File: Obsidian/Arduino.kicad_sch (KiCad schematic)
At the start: 25 parts

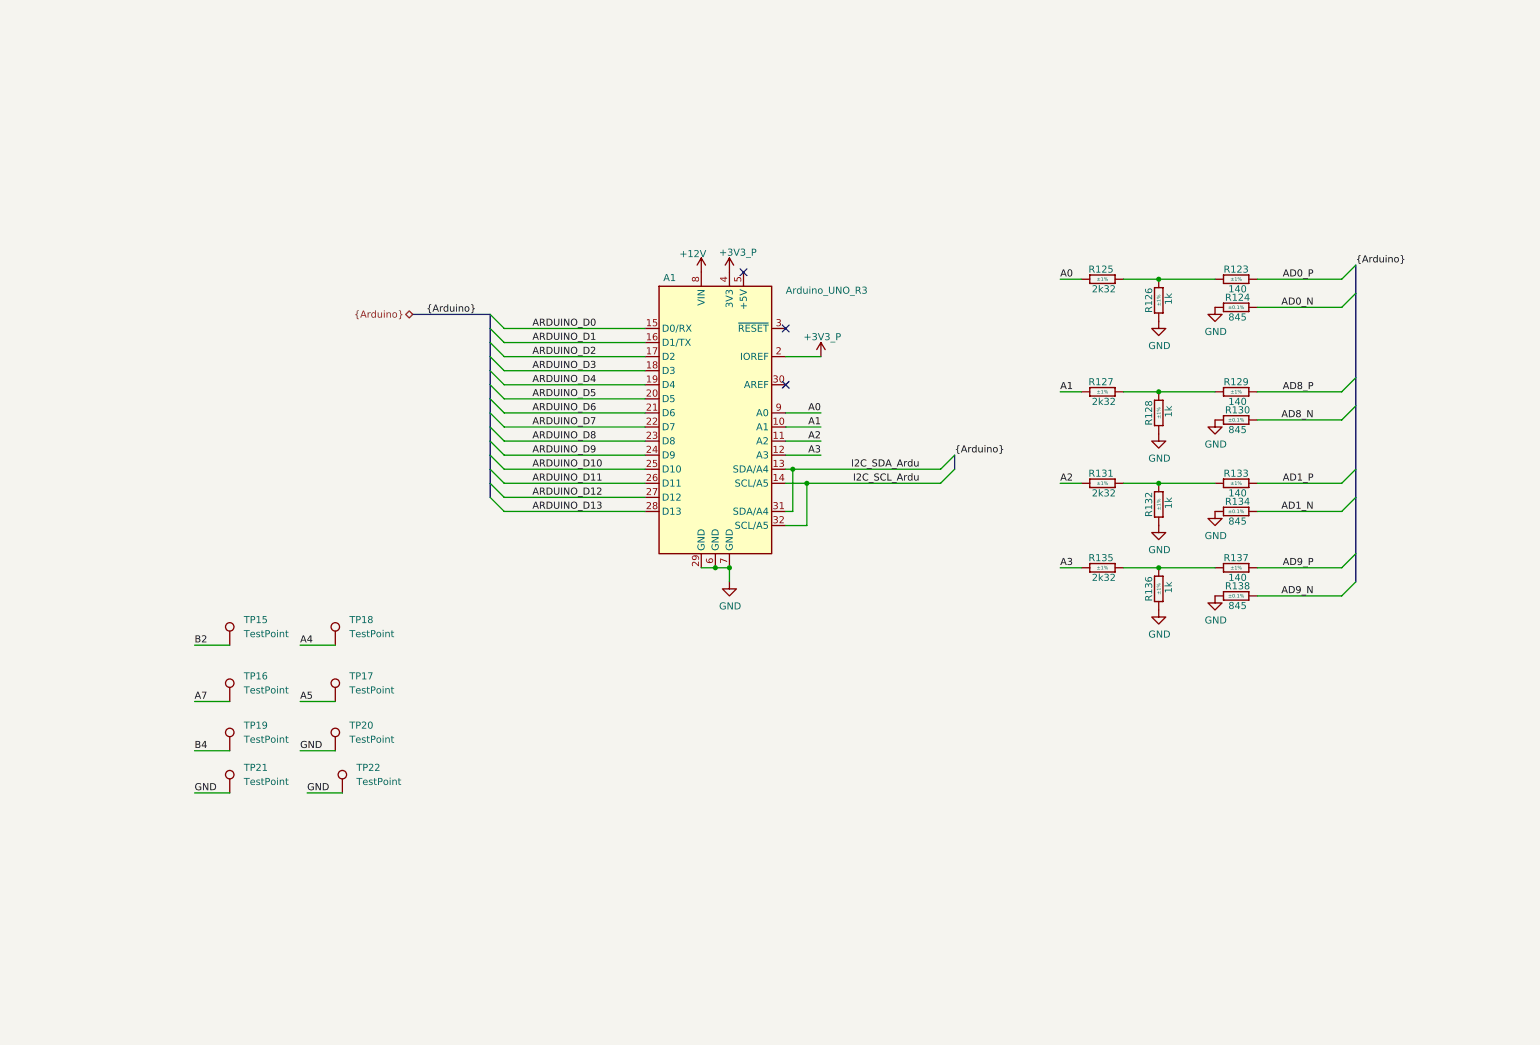
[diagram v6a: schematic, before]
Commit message: adding flex connector
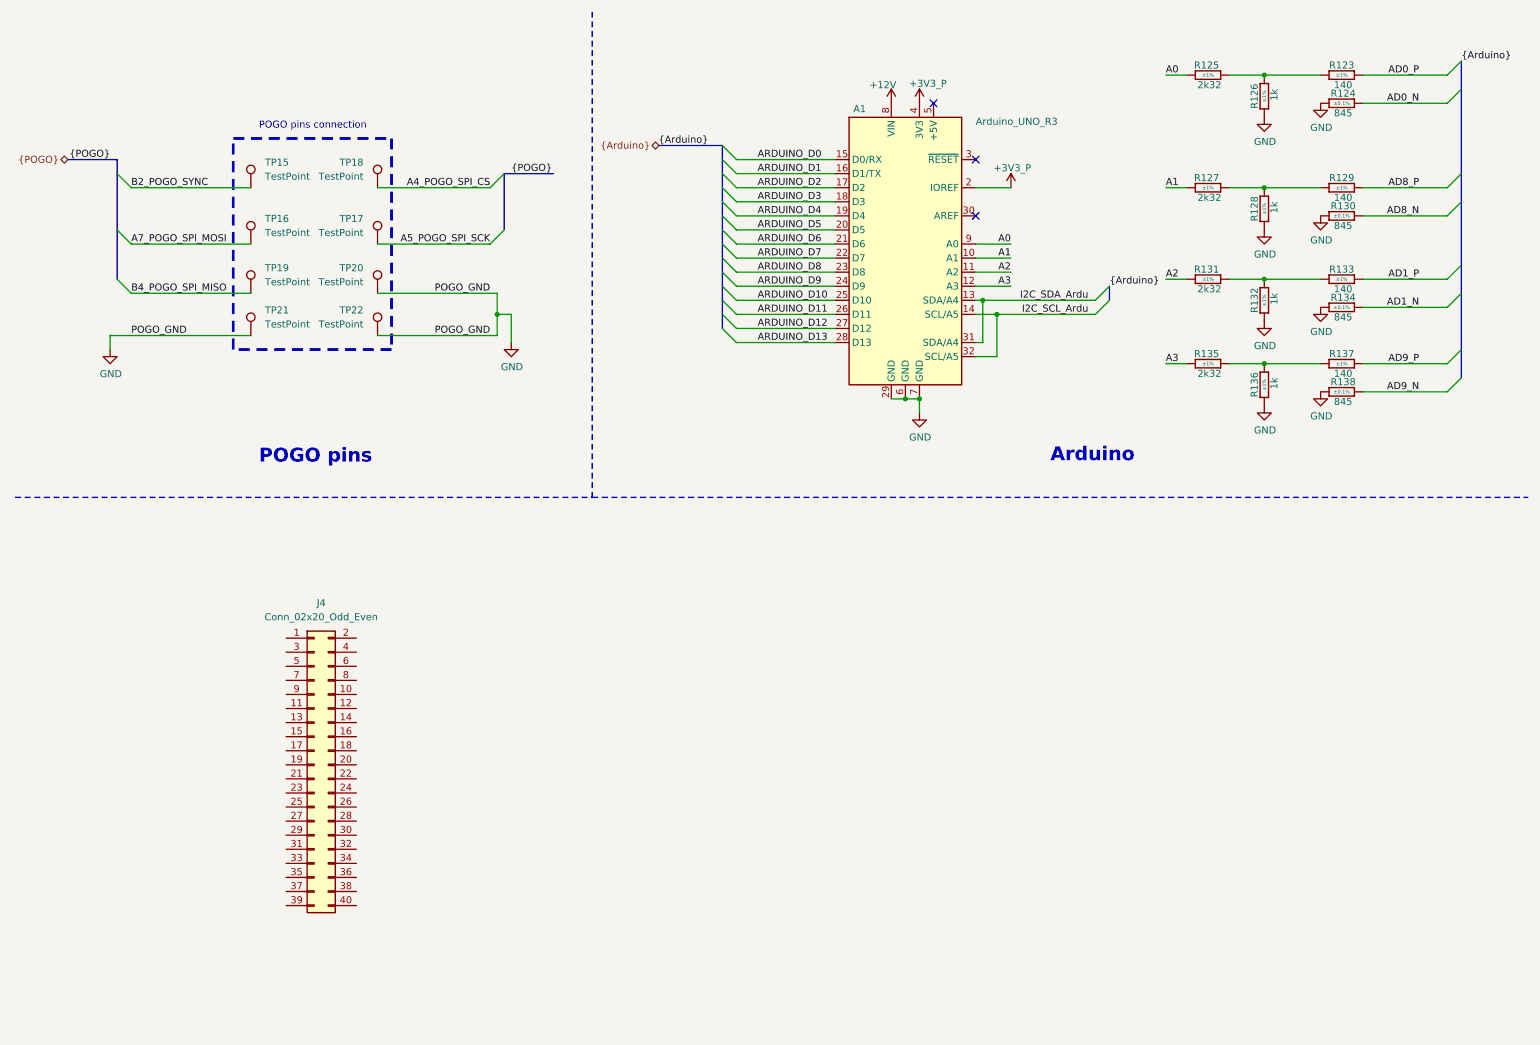
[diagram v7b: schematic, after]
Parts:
- added J4: Conn_02x20_Odd_Even, Footprint:CONN-SMD_YXT-BB10-40S-02, symbol Connector_Generic:Conn_02x20_Odd_Even
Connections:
- net A4 renamed A4_POGO_SPI_CS
- net A5 renamed A5_POGO_SPI_SCK
- net A7 renamed A7_POGO_SPI_MOSI
- net B2 renamed B2_POGO_SYNC
- net B4 renamed B4_POGO_SPI_MISO
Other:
- note added: "Arduino"
- note added: "POGO pins"
- note added: "POGO pins connection"
- moved on the sheet: A1, R123, R124, R125, R126, R127, R128, R129, R130, R131, R132, R133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

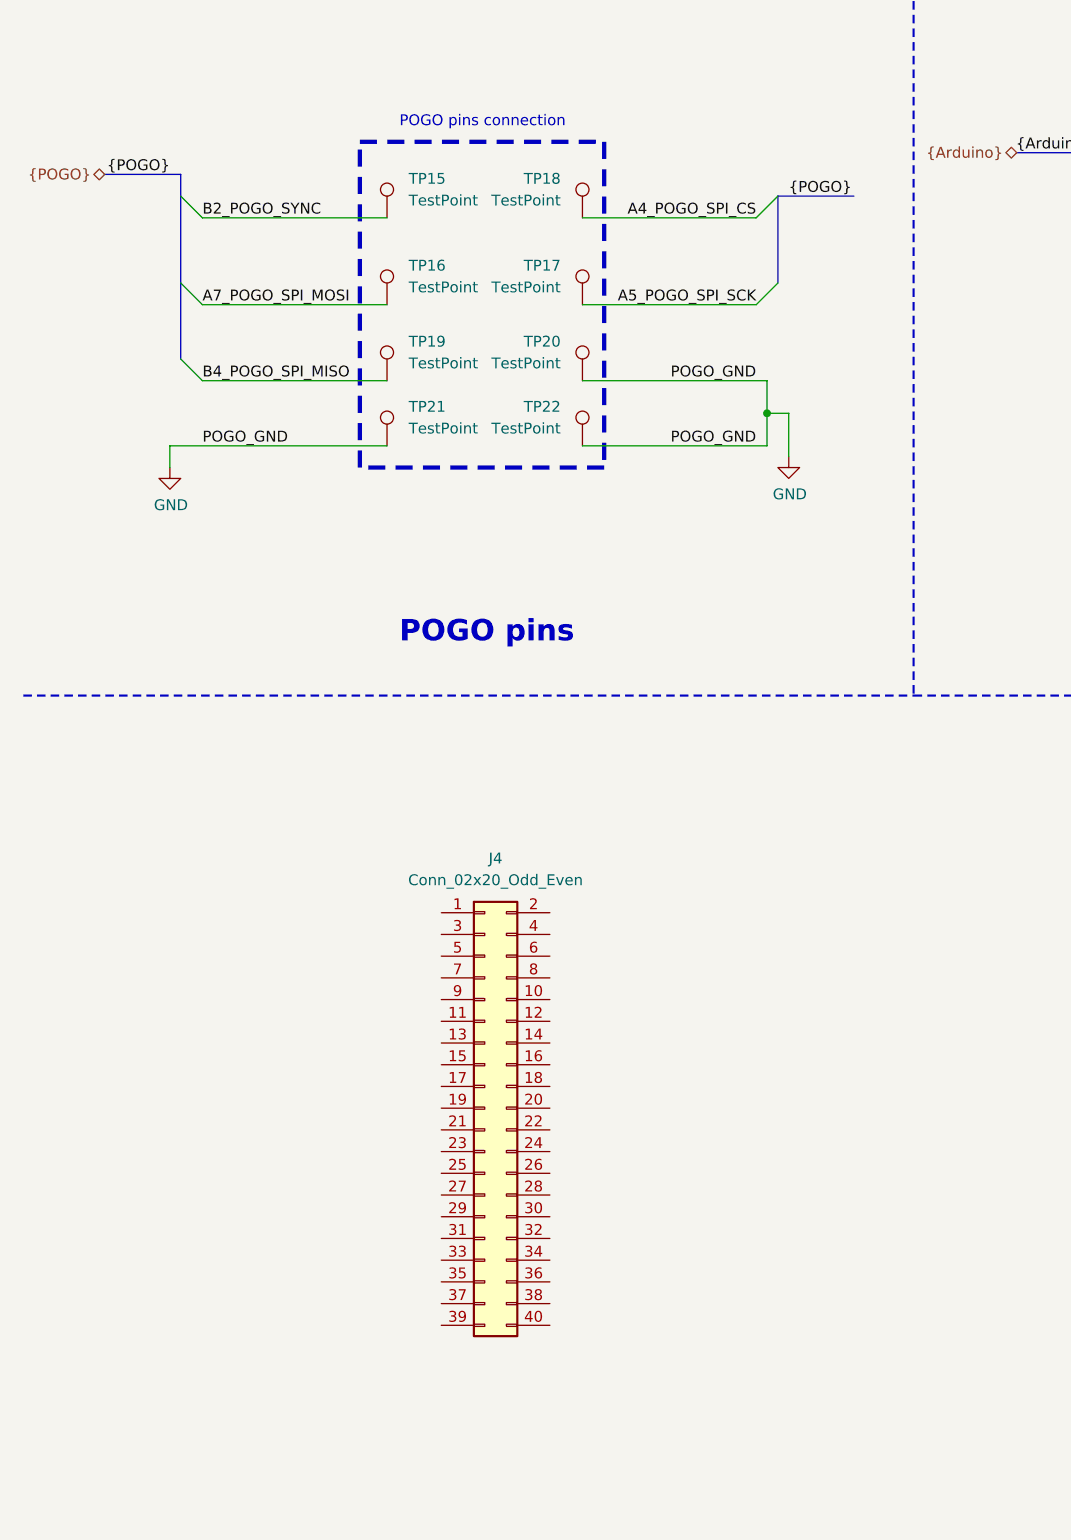
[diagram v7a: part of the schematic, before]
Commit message: Cleanup of the schematic
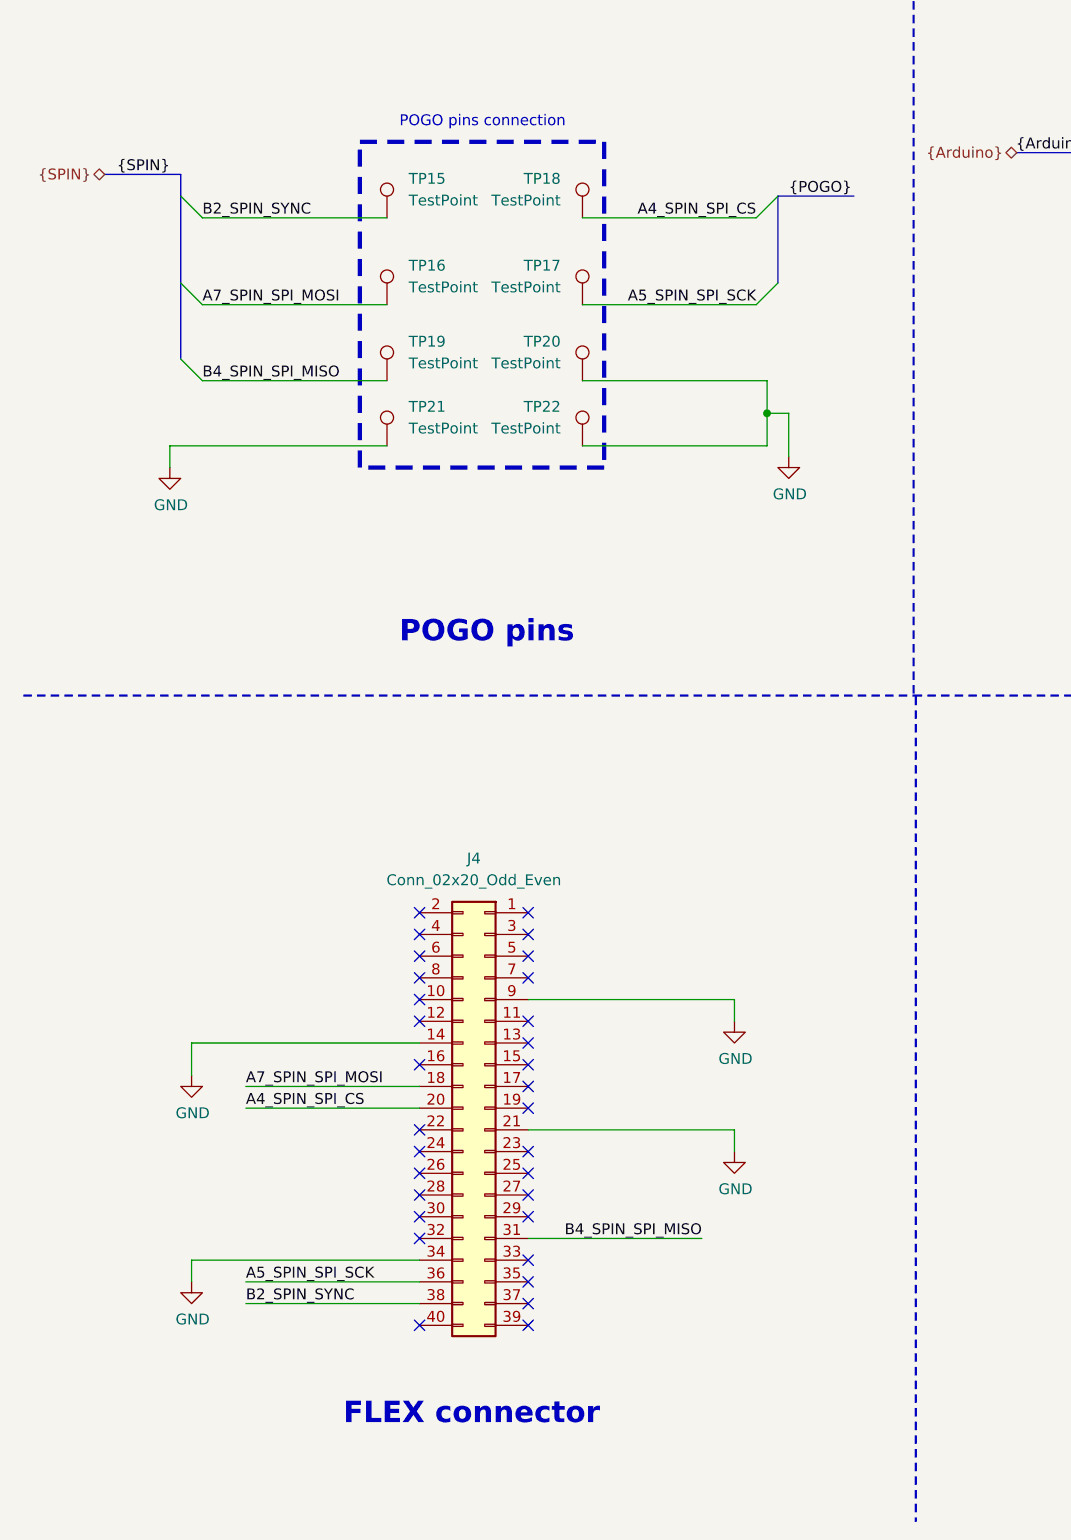
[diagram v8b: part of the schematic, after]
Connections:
- net A4_POGO_SPI_CS is gone; now on net A4_SPIN_SPI_CS: TP18.1
- net A5_POGO_SPI_SCK is gone; now on net A5_SPIN_SPI_SCK: TP17.1
- net A7_POGO_SPI_MOSI is gone; now on net A7_SPIN_SPI_MOSI: TP16.1
- net B2_POGO_SYNC is gone; now on net B2_SPIN_SYNC: TP15.1
- net B4_POGO_SPI_MISO is gone; now on net B4_SPIN_SPI_MISO: TP19.1
- net GND: now also J4.14 (Pin_14), J4.21 (Pin_21), J4.34 (Pin_34), J4.9 (Pin_9)
- net A7_SPIN_SPI_MOSI: now reaches J4.18 (Pin_18)
- net A4_SPIN_SPI_CS: now reaches J4.20 (Pin_20)
- net B4_SPIN_SPI_MISO: now reaches J4.31 (Pin_31)
- net A5_SPIN_SPI_SCK: now reaches J4.36 (Pin_36)
- net B2_SPIN_SYNC: now reaches J4.38 (Pin_38)
- no-connect marks 3 -> 34
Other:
- note added: "FLEX connector"
- moved on the sheet: J4
